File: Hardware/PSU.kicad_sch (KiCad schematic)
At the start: 21 parts, among them SW1 SW_SPDT, SW2 SW_SPDT, U4 TLV74115_SOT23-5, U5 TLV74133_SOT23-5

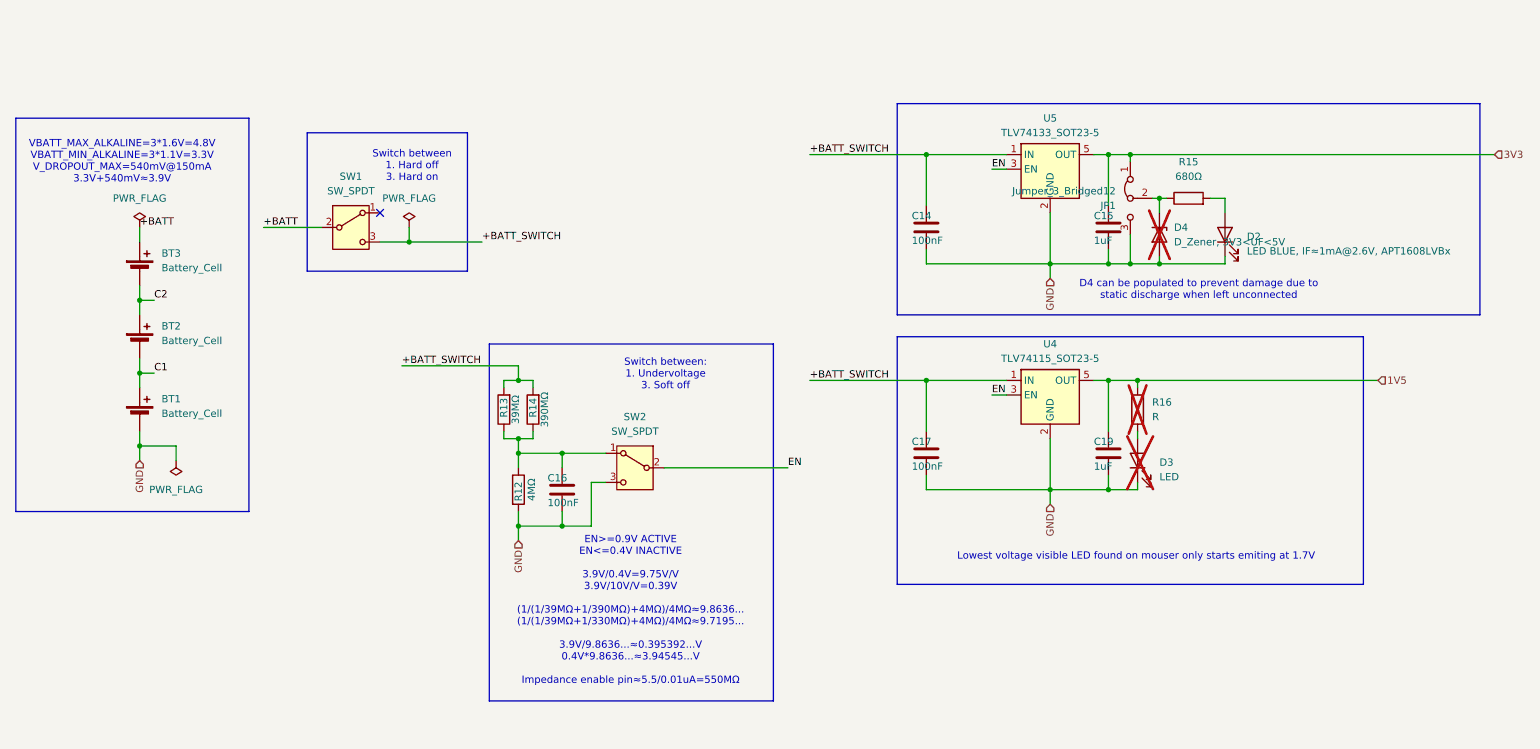
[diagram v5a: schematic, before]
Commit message: added more footprints and continued on the circuit diagram
- [ ] add antenna connection
- [ ] find suitable 390Mohm resistor
- [ ] add switches, reset and power
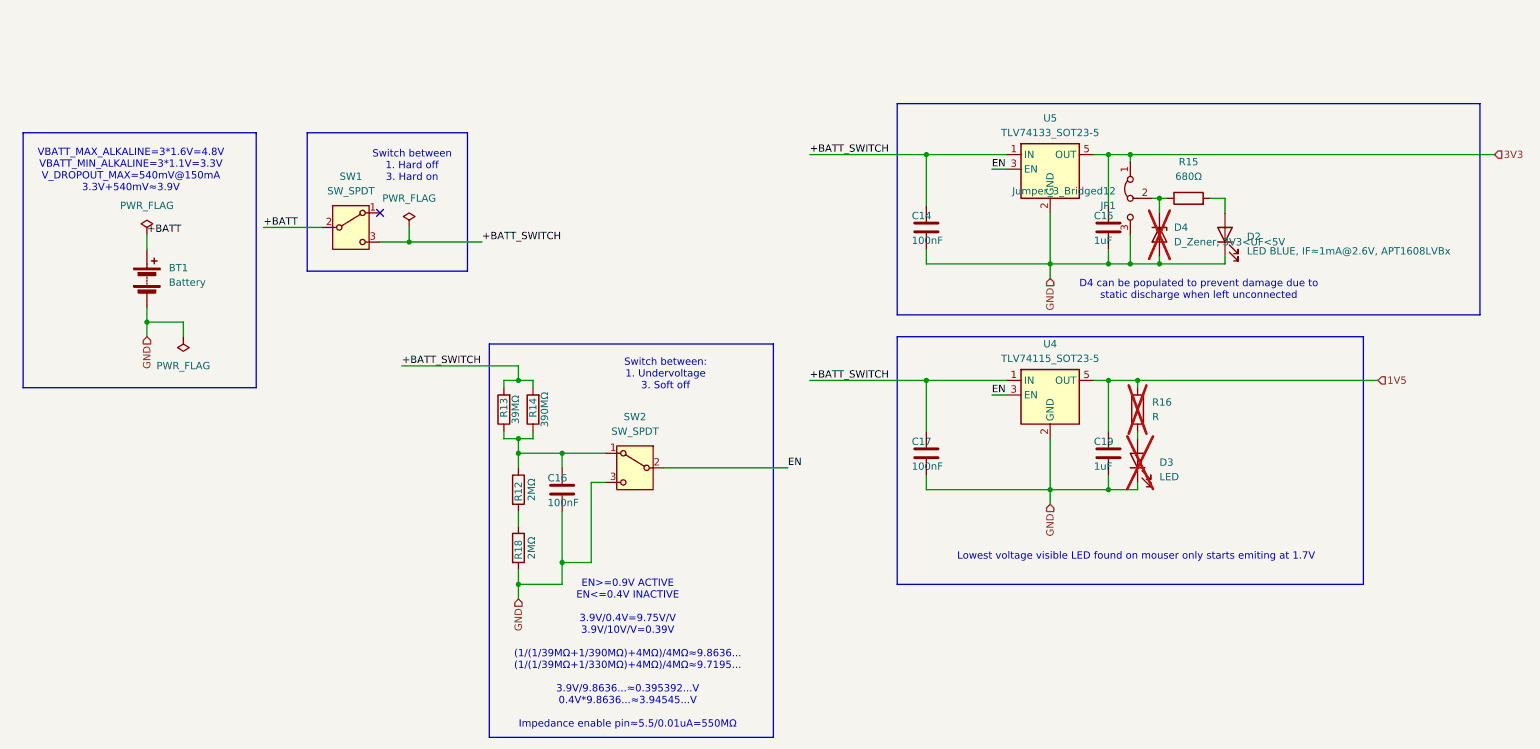
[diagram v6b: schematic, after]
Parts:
- removed BT1, BT2, BT3: Battery_Cell, symbol Device:Battery_Cell
- added BT1: Battery, Battery:BatteryHolder_Keystone_2479_3xAAA, symbol Device:Battery
- added R18: 2MΩ, Resistor_SMD:R_0402_1005Metric_Pad0.72x0.64mm_HandSolder, symbol Device:R
- D2: footprint (none) -> LED_SMD:LED_0603_1608Metric_Pad1.05x0.95mm_HandSolder
- D4: now left out of the parts list
- R12: value 4MΩ -> 2MΩ; footprint (none) -> Resistor_SMD:R_0402_1005Metric_Pad0.72x0.64mm_HandSolder
- R13: footprint (none) -> Resistor_SMD:R_0402_1005Metric_Pad0.72x0.64mm_HandSolder
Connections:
- net +BATT: now also BT1.1 (+)
- net GND: now also BT1.2 (-), R18.2; no longer R12.2
- new net: R12.2, R18.1

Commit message: PCB is done???
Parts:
- R14: value 390MΩ -> 330MΩ preferably 390MΩ; footprint (none) -> Resistor_SMD:R_0603_1608Metric_Pad0.98x0.95mm_HandSolder
- SW1: value SW_SPDT -> Power_Hard; footprint (none) -> Button_Switch_SMD:SW_SPDT_PCM12
- SW2: value SW_SPDT -> Power_Soft; footprint (none) -> Button_Switch_SMD:SW_SPDT_PCM12
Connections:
- net +BATT: now also SW1.3 (C); no longer SW1.2 (B)
- net +BATT_SWITCH: now also SW1.2 (B); no longer SW1.3 (C)
- net GND: now also SW2.1 (A); no longer SW2.3 (C)
- net at C16.1, R12.1, R13.1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: now also SW2.3 (C); no longer SW2.1 (A)
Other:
- moved on the sheet: SW1, SW2
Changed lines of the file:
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@@
 	)
 	(no_connect
-		(at 81.28 48.26)
+		(at 71.12 50.8)
 	)
 	(wire
@@
 	(wire
 		(pts
-			(xy 60.96 50.8) (xy 71.12 50.8)
-		)
-		(stroke
-			(width 0)
-			(type default)
-		)
-	)
-	(wire
-		(pts
 			(xy 212.09 38.1) (xy 208.28 38.1)
 		)
@@
 		(pts
 			(xy 102.87 78.74) (xy 102.87 77.47)
+		)
+		(stroke
+			(width 0)
+			(type default)
+		)
+	)
+	(wire
+		(pts
+			(xy 60.96 55.88) (xy 71.12 55.88)
 		)
 		(stroke
@@
 	)
 	(label "+BATT"
-		(at 60.96 50.8 0)
+		(at 60.96 55.88 0)
 		(effects
 			(font
@@
 	(symbol
 		(lib_id "Switch:SW_SPDT")
-		(at 76.2 50.8 0)
+		(at 76.2 53.34 0)
+		(mirror y)
 		(unit 1)
 		(exclude_from_sim no)
@@
 		(on_board yes)
 		(dnp no)
-		(fields_autoplaced yes)
 		(property "Reference" "SW1"
-			(at 76.2 41.91 0)
-			(effects
-				(font
-					(size 1.27 1.27)
-				)
-			)
-		)
-		(property "Value" "SW_SPDT"
 			(at 76.2 44.45 0)
 			(effects
@@
 			)
 		)
-		(property "Footprint" ""
-			(at 76.2 50.8 0)
+		(property "Value" "Power_Hard"
+			(at 76.2 46.99 0)
+			(effects
+				(font
+					(size 1.27 1.27)
+				)
+			)
+		)
+		(property "Footprint" "Button_Switch_SMD:SW_SPDT_PCM12"
+			(at 76.2 53.34 0)
 			(effects
 				(font
@@
 		)
 		(property "Datasheet" "~"
-			(at 76.2 58.42 0)
+			(at 76.2 60.96 0)
 			(effects
 				(font
@@
 		)
 		(property "Description" "Switch, single pole double throw"
-			(at 76.2 50.8 0)
+			(at 76.2 53.34 0)
 			(effects
 				(font
@@
 	(symbol
 		(lib_id "Switch:SW_SPDT")
-		(at 125.73 92.71 0)
-		(mirror y)
+		(at 125.73 92.71 180)
 		(unit 1)
 		(exclude_from_sim no)
@@
 		(dnp no)
 		(property "Reference" "SW2"
-			(at 125.73 83.82 0)
-			(effects
-				(font
-					(size 1.27 1.27)
-				)
-			)
-		)
-		(property "Value" "SW_SPDT"
-			(at 125.73 86.36 0)
-			(effects
-				(font
-					(size 1.27 1.27)
-				)
-			)
-		)
-		(property "Footprint" ""
+			(at 125.73 101.6 0)
+			(effects
+				(font
+					(size 1.27 1.27)
+				)
+			)
+		)
+		(property "Value" "Power_Soft"
+			(at 125.73 99.06 0)
+			(effects
+				(font
+					(size 1.27 1.27)
+				)
+			)
+		)
+		(property "Footprint" "Button_Switch_SMD:SW_SPDT_PCM12"
 			(at 125.73 92.71 0)
 			(effects
@@
 		)
 		(property "Datasheet" "~"
-			(at 125.73 100.33 0)
+			(at 125.73 85.09 0)
 			(effects
 				(font
@@
 			)
 		)
-		(property "Value" "390MΩ"
+		(property "Value" "330MΩ preferably 390MΩ"
 			(at 109.982 82.55 90)
 			(effects
@@
 			)
 		)
-		(property "Footprint" ""
+		(property "Footprint" "Resistor_SMD:R_0603_1608Metric_Pad0.98x0.95mm_HandSolder"
 			(at 109.728 82.55 90)
 			(effects

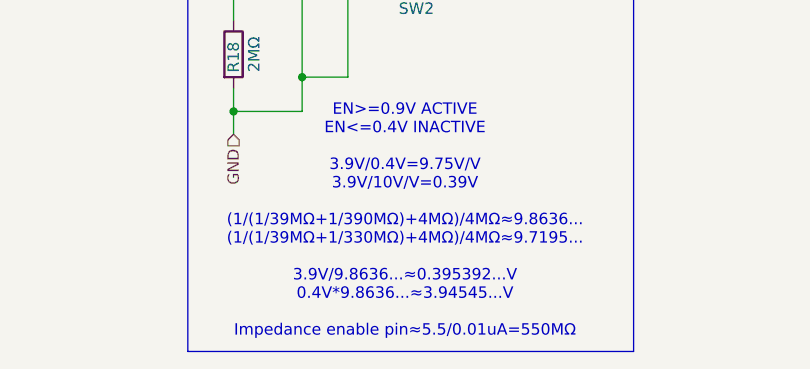
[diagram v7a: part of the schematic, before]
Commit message: Changed text to match resistor values for regulator enable divider
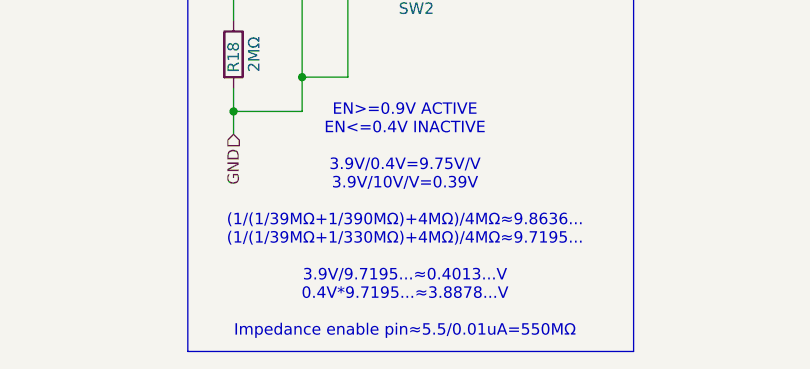
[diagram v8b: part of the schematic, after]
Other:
- note added: "EN>=0.9V ACTIVE EN<=0.4V INACTIVE 3.9V/0.4V=9.75V/V 3.9V/10V/V=0.39V (1/(1/39MΩ+1/390MΩ)+4MΩ)/4MΩ≈9.8636... (1/(1/39MΩ+1/330MΩ)+4MΩ)/4MΩ≈9.7195... 3.9V/9.7195...≈0.4013...V 0.4V*9.7195...≈3.8878...V Impedance enable pin≈5.5/0.01uA=550MΩ"
- note removed: "EN>=0.9V ACTIVE EN<=0.4V INACTIVE 3.9V/0.4V=9.75V/V 3.9V/10V/V=0.39V (1/(1/39MΩ+1/390MΩ)+4MΩ)/4MΩ≈9.8636... (1/(1/39MΩ+1/330MΩ)+4MΩ)/4MΩ≈9.7195... 3.9V/9.8636...≈0.395392...V 0.4V*9.8636...≈3.94545...V Impedance enable pin≈5.5/0.01uA=550MΩ"
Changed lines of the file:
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@@
 		)
 	)
-	(text "EN>=0.9V ACTIVE\nEN<=0.4V INACTIVE\n\n3.9V/0.4V=9.75V/V\n3.9V/10V/V=0.39V\n\n(1/(1/39MΩ+1/390MΩ)+4MΩ)/4MΩ≈9.8636...\n(1/(1/39MΩ+1/330MΩ)+4MΩ)/4MΩ≈9.7195...\n\n3.9V/9.8636...≈0.395392...V\n0.4V*9.8636...≈3.94545...V\n\nImpedance enable pin≈5.5/0.01uA=550MΩ"
+	(text "EN>=0.9V ACTIVE\nEN<=0.4V INACTIVE\n\n3.9V/0.4V=9.75V/V\n3.9V/10V/V=0.39V\n\n(1/(1/39MΩ+1/390MΩ)+4MΩ)/4MΩ≈9.8636...\n(1/(1/39MΩ+1/330MΩ)+4MΩ)/4MΩ≈9.7195...\n\n3.9V/9.7195...≈0.4013...V\n0.4V*9.7195...≈3.8878...V\n\nImpedance enable pin≈5.5/0.01uA=550MΩ"
 		(exclude_from_sim no)
 		(at 124.46 125.222 0)
